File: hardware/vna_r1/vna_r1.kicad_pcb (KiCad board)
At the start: 2 copper layers, 668 parts, among them IC1301 SN74LVC1G07DCK, IC1302 TPD4S012DRYR, IC1303 TPD4S012DRYR, J1202 BARREL_JACK, J1301 RJ45-TRANSFO, J1302 USB_A, J201 BMI-S-209, J401 RF_Shield_Two_Pieces, J402 RF_Shield_Two_Pieces, J501 RF_Shield_Two_Pieces, J601 RF_Shield_Two_Pieces, J701 RF_Shield_Two_Pieces, J801 RF_Shield_Two_Pieces, J901 CONN_01X02, Q1201 Q_PMOS_DGS, Q1301 24 MHz, Q1302 24 MHz, T501 Transformer_SP_1S, T601 Transformer_SP_1S, T701 Transformer_SP_1S, T801 Transformer_SP_1S, U1001 CONN_SMA, U1002 CONN_SMA, U1003 CONN_SMA_2GND, U1004 CONN_SMA_2GND, U1005 CONN_SMA_2GND, U1006 CONN_SMA_2GND, U1007 CONN_SMA_2GND, U1008 CONN_SMA_2GND, U1101 AD9577, U1102 NB3N551, U1201 CONN_SMA, U1202 CONN_SMA, U1301 OSD3358-512M-BSM, U1302 74HC244, U1303 LAN8710A, U1304 TPS2051, U1305 MICROSD, U201 LMX2594, U301 LMX2594, U302 LTC2630, U303 ADRF5040, U304 LTC2054HV, U305 MAAM-011100, U401 NC7WZU04, U402 PE42521, U403 MASW-008322-TR1000, U404 PE42521, U501 LTC5549, U502 ad9864, U601 LTC5549, U602 ad9864, U701 LTC5549, U702 ad9864, U801 LTC5549, U802 ad9864, U901 ADP7158, U902 ADP7158, U903 ADP7158, U904 OKR-T/3-W12-C, U905 TPS2041B, U906 LTC1983, X1301 10118192-0001LF, Y1101 26 MHz 7M-26.000MEEQ-T

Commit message: more layout on vna r1
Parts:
- removed C1323, C1326: 100 nF, Capacitors_SMD:C_0402
- added C227: 10 pF, Capacitors_SMD:C_0603, F.Cu at (582.0, 158.0)
- added R213: 51, Resistors_SMD:R_0402, F.Cu at (581.2, 159.9)
- moved C1201 157.0 mm to (351.7, 73.7)
- moved C1202 157.0 mm to (348.5, 88.5)
- moved C901 157.0 mm to (379.8, 88.0)
- moved C902 157.0 mm to (380.0, 31.0)
- moved C903 157.0 mm to (376.8, 57.0)
- moved C904 157.0 mm to (381.3, 36.0)
- moved C905 157.0 mm to (381.9, 54.0)
- moved C906 157.0 mm to (383.2, 81.0)
- moved C907 157.0 mm to (397.2, 33.0)
- moved C908 157.0 mm to (392.8, 60.0)
- moved C909 157.0 mm to (395.8, 90.0)
- moved C910 157.0 mm to (396.2, 29.0)
- moved C911 157.0 mm to (394.8, 53.0)
- moved C912 157.0 mm to (402.2, 90.0)
- moved C913 157.0 mm to (392.8, 31.0)
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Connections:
- RN1305 pad 1: /control/MMC0_D2 -> /control/MMC0_CLK
- RN1305 pad 2: /control/MMC0_D3 -> /control/MMC0_CMD
- RN1305 pad 3: /control/MMC0_CMD -> /control/MMC0_D3
- RN1305 pad 4: /control/MMC0_CLK -> /control/MMC0_D2
- RN1306 pad 1: /control/MMC0_D0 -> (no net)
- RN1306 pad 2: /control/MMC0_D1 -> /control/MMC0_CD
- RN1306 pad 3: /control/MMC0_CD -> /control/MMC0_D1
- RN1306 pad 4: (no net) -> /control/MMC0_D0
- RN201 pad 1: /LO_SYNTH_LOCK -> /LO_SYNTH_CE
- RN201 pad 2: /LO_SPI_SDI -> /LO_SPI_CLK
- RN201 pad 3: /LO_SPI_CLK -> /LO_SPI_SDI
- RN201 pad 4: /LO_SYNTH_CE -> /LO_SYNTH_LOCK
- RN201 pad 5: /LO_SYNTH_CE -> /LO_SYNTH_LOCK
- RN201 pad 6: /LO_SPI_CLK -> /LO_SPI_SDI
- RN201 pad 7: /LO_SPI_SDI -> /LO_SPI_CLK
- RN201 pad 8: /LO_SYNTH_LOCK -> /LO_SYNTH_CE
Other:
- copper layers 2 -> 4
- rule pad_to_mask_clearance: 0.2 -> 0.05

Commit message: layout on vna r1 control board
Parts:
- removed C201, C202, C217, C301, C302, C317, C332, C333, C335, C339, C344, C346, C401, C405, C406, C503, C603, C703, C803, C918, C920, C922, C924, C925: 100 nF, Capacitors_SMD:C_0402
- removed C203, C206, C207, C208, C209, C210, C221, C303, C306, C307, C308, C309, C310, C320, C904, C907, C910, C923: 1 uF, Capacitors_SMD:C_0402
- removed C204, C211, C214, C218, C219, C304, C311, C312, C318, C319, C902, C913, C919, C921: 10 uF, Capacitors_SMD:C_0603
- removed C205, C220, C222, C223, C224, C227: 10 pF, Capacitors_SMD:C_0603
- removed C212, C315: DNP, Capacitors_SMD:C_0402
- removed C213, C316: 1800 pF, Capacitors_SMD:C_0402
- removed C215, C313: 390 pF, Capacitors_SMD:C_0402
- removed C216, C314: 68 nF, Capacitors_SMD:C_0402
- removed C225, C226, C321, C322: 10 nF, Capacitors_SMD:C_0402
- removed C305, C323, C324, C325, C326, C327, C328, C329, C330, C331, C334, C336, C337, C338, C340, C341, C342, C347, C348, C402, C403, C404, C407, C408, C409, C410, C412, C414, C501, C502, C505, C506, C507, C601, C602, C605, C606, C607, C701, C702, C705, C706, C707, C801, C802, C805, C806, C807: 10 pF, Capacitors_SMD:C_0402
- removed C343, C345: 220 nF, Capacitors_SMD:C_0402
- removed C411, C413: 1 uF, Capacitors_SMD:C_0805
- removed C926: 100 pF, Capacitors_SMD:C_0402
- removed D1001, D1002, D201: RED, LEDs:LED_0603
- removed D301, D302, D303: LED_Small, LEDs:LED_0603
- removed D401: 5.1V, Diodes_SMD:SOD-323
- removed D402: LED, LEDs:LED_0603
- removed FL301: 5515LP15A730, vna_footprints:5515LP15A730
- removed FL302: 1810LP07A200, vna_footprints:1810LP07A200
- removed FL303: 3550LP14A300, vna_footprints:3550LP14A300
- removed J201: BMI-S-209, Shielding_Cabinets:Laird_Technologies_BMI-S-209-F_29.36x18.50mm
- removed J401, J402: RF_Shield_Two_Pieces, Shielding_Cabinets:Laird_Technologies_BMI-S-202-F_16.50x16.50mm
- removed J501, J601, J801: RF_Shield_Two_Pieces, Shielding_Cabinets:Laird_Technologies_BMI-S-209-F_29.36x18.50mm
- removed L201, L202, L301, L302: 22 nH, Resistors_SMD:R_0402
- removed L303, L501, L601, L701, L801: BLM15GG471, Resistors_SMD:R_0402
- removed L401, L402: 506WLSN6R00KT236T, vna_footprints:ATC506WLS
- removed L901: L_Small, Resistors_SMD:R_0805
- removed R201, R205, R304, R324: JMP, Resistors_SMD:R_0402
- removed R202, R301, R403, R404: 100, Resistors_SMD:R_0402
- removed R203, R204, R302, R303, R312, R313, R316, R317, R318, R328, R401, R402, R405, R407, R502, R503, R602, R603, R702, R703, R802, R803: 1k, Resistors_SMD:R_0402
- removed R206, R305: 18, Resistors_SMD:R_0402
- removed R207, R306: 68, Resistors_SMD:R_0402
- removed R208, R314, R315, R327, R905, R906: 10k, Resistors_SMD:R_0402
- removed R209, R210, R211, R212, R213, R308, R309, R310, R311, R406, R408: 51, Resistors_SMD:R_0402
- removed R307: 0, Resistors_SMD:R_0402
- removed R319: 9.1k, Resistors_SMD:R_0402
- removed R320: 4.7k, Resistors_SMD:R_0402
- removed R321, R322, R323: DNP, Resistors_SMD:R_0402
- removed R325: 2k, Resistors_SMD:R_0402
- removed R326: 18k, Resistors_SMD:R_0402
- removed R329: 56.2k, Resistors_SMD:R_0402
- removed R330: 68k, Resistors_SMD:R_0402
- removed RN1304: 49.9, pocketbeagle:RN0804
- removed RN201, RN301: RESISTOR.NETWORK-_4_, pocketbeagle:RN0804
- removed T501, T601, T701, T801: Transformer_SP_1S, vna_footprints:5LEAD_BALUN_4p83mm_3p3mm
- removed U1001, U1002: CONN_SMA, vna_footprints:732511150_sma_thin
- removed U1007, U1008: CONN_SMA_2GND, vna_footprints:SMA_901-10512_6p7MIL_FR408_CPW_LAUNCH
- removed U201, U301: LMX2594, Housings_DFN_QFN:QFN-40-1EP_6x6mm_Pitch0.5mm
- removed U302: LTC2630, TO_SOT_Packages_SMD:SC-70-6
- removed U303: ADRF5040, Housings_DFN_QFN:QFN-24-1EP_4x4mm_Pitch0.5mm
- removed U304: LTC2054HV, TO_SOT_Packages_SMD:SOT-23-5
- removed U305: MAAM-011100, vna_footprints:TDFN6
- removed U401: NC7WZU04, TO_SOT_Packages_SMD:SC-70-6
- removed U402, U404: PE42521, Housings_DFN_QFN:QFN-16-1EP_3x3mm_Pitch0.5mm
- removed U403: MASW-008322-TR1000, Housings_DFN_QFN:QFN-24-1EP_4x4mm_Pitch0.5mm
- removed U501, U601, U701, U801: LTC5549, vna_footprints:QFN_12_3mm2mm
- removed U901: ADP7158, Housings_DFN_QFN:DFN-10-1EP_3x3mm_Pitch0.5mm
- removed U905: TPS2041B, TO_SOT_Packages_SMD:SOT-23-5
- removed U906: LTC1983, TO_SOT_Packages_SMD:SOT-23-6
- added H901: MOUNTING_HOLE, Mounting_Holes:MountingHole_2-7mm, F.Cu at (297.6, -102.4)
- added H902: MOUNTING_HOLE, Mounting_Holes:MountingHole_2-7mm, F.Cu at (423.5, -109.5)
- added H903: MOUNTING_HOLE, Mounting_Holes:MountingHole_2-7mm, F.Cu at (422.4, -185.4)
- added H904: MOUNTING_HOLE, Mounting_Holes:MountingHole_2-7mm, F.Cu at (309.0, -183.6)
- added J1201: DB15_FEMALE_MountingHoles, Connect:DB15FD, F.Cu at (409.4, -89.4)
- added R1004: 51, Resistors_SMD:R_0402, F.Cu at (314.2, -146.7)
- added R1005: 51, Resistors_SMD:R_0402, F.Cu at (314.2, -143.8)
- C1314, RN1305, RN1306: moved to B.Cu
- J1301: value RJ45-TRANSFO -> 0480254000; footprint Connect:RJHSE538X -> Connect:RJ45_TRANSFO
- J701: value RF_Shield_Two_Pieces -> Conn_01x07; footprint Shielding_Cabinets:Laird_Technologies_BMI-S-209-F_29.36x18.50mm -> Connect:Wafer_Horizontal20x5.8x7RM2.5-7
- R1001, R1002: value 1k -> 51
- TP1301, TP1302, TP1303, TP1304, TP1305, TP1306, TP1307, TP1308, TP1309, TP1310: footprint pocketbeagle:TP07R -> vna_footprints:TP07R
- moved U1006 459.4 mm to (409.3, -195.3), turned to 90 degrees
- moved R1002 457.7 mm to (314.2, -149.2), turned to 90 degrees
- moved R1001 448.1 mm to (314.2, -151.7), turned to 270 degrees
- moved C804 439.5 mm to (394.5, -186.3), turned to 90 degrees
- moved D1003 438.1 mm to (319.1, -115.1), turned to 90 degrees
- moved R1003 436.4 mm to (318.8, -112.1), turned to 270 degrees
- moved C808 433.9 mm to (400.8, -184.3)
- moved R805 431.6 mm to (400.0, -181.4), turned to 90 degrees
- moved C823 430.6 mm to (407.6, -174.4)
- moved R801 429.8 mm to (394.5, -183.6), turned to 270 degrees
- moved R806 427.1 mm to (404.0, -176.7), turned to 180 degrees
- moved R812 424.8 mm to (389.8, -167.5), turned to 180 degrees
- moved C824 422.4 mm to (412.8, -175.5), turned to 90 degrees
- moved C815 422.3 mm to (405.0, -168.9), turned to 180 degrees
- moved C813 420.4 mm to (403.3, -171.3), turned to 270 degrees
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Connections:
- C504 pad 2: Net-(C504-Pad2) -> /front_panel/DEMOD_1
- C604 pad 2: Net-(C604-Pad2) -> /front_panel/DEMOD_2
- C704 pad 2: Net-(C704-Pad2) -> /front_panel/DEMOD_3
- C804 pad 2: Net-(C804-Pad2) -> /front_panel/DEMOD_4
- J701 pad 1: GND -> (no net)
- L1304 pad 2: (no net) -> Net-(J1301-Pad13)
- R1001 pad 1: Net-(D1001-Pad1) -> Net-(C1311-Pad1)
- R1001 pad 2: GND -> /control/RX_N
- R1002 pad 1: Net-(D1002-Pad1) -> Net-(C1311-Pad1)
- R1002 pad 2: GND -> /control/RX_P
- R1355 pad 2: (no net) -> Net-(J1301-PadGK)
- R1356 pad 2: (no net) -> Net-(J1301-PadYK)
- U1101 pad 17: /SYNTH_REF_AN -> (no net)
- U1101 pad 18: /SYNTH_REF_AP -> (no net)
- U1101 pad 22: /SYNTH_REF_BN -> (no net)
- U1101 pad 23: /SYNTH_REF_BP -> (no net)
- U1301 pad A10: /RF_AMP_EN -> (no net)
- U1301 pad A13: (no net) -> /EXT_SPI_MOSI
- U1301 pad A14: (no net) -> /EXT_SPI_CS0
- U1301 pad A2: /RF_SYNTH_CS -> (no net)
- U1301 pad A3: /LO_SPI_CLK -> (no net)
- U1301 pad B1: /RF_DAC_CS -> (no net)
- U1301 pad B13: (no net) -> /EXT_SPI_MISO
- U1301 pad B14: (no net) -> /EXT_SPI_CLK
- U1301 pad B2: /LO_SYNTH_CS -> (no net)
- U1301 pad B3: /LO_SPI_SDI -> (no net)
- U1301 pad B4: /-5V_EN -> (no net)
- U1301 pad C12: /3V3_RF_EN -> (no net)
- U1301 pad C3: /RF_SPI_CLK -> (no net)
- U1301 pad C4: /RF_SPI_SDI -> (no net)
- U1301 pad C8: (no net) -> /EXT_AIN0
- U1301 pad C9: (no net) -> /EXT_AIN1
- U1301 pad E1: (no net) -> Net-(TP1308-Pad1)
- U1301 pad F13: (no net) -> Net-(TP1303-Pad1)
- U1301 pad F2: (no net) -> Net-(TP1307-Pad1)
- U1301 pad F4: (no net) -> Net-(TP1301-Pad1)
- U1301 pad G13: (no net) -> Net-(TP1304-Pad1)
- U1301 pad G4: (no net) -> Net-(TP1302-Pad1)
- U1301 pad N13: (no net) -> Net-(TP1309-Pad1)
- U1301 pad P1: (no net) -> /EXT_IO_2
- U1301 pad P2: (no net) -> /EXT_IO_1
- U1301 pad P3: (no net) -> /EXT_IO_0
- U1301 pad P4: /LO_SYNTH_LOCK -> (no net)
- U1301 pad R1: /RF_FILT_SW_1 -> (no net)
- U1301 pad R12: /MIX_EN -> (no net)
- U1301 pad R13: /PANEL_PORT1_LED -> (no net)
- U1301 pad R4: /LO_SYNTH_CE -> (no net)
- U1301 pad R7: (no net) -> /EXT_IO_3
- U1301 pad T1: /RF_SYNTH_LOCK -> (no net)
- U1301 pad T12: /MIX_X2 -> (no net)
- U1301 pad T15: /PANEL_PORT2_LED -> (no net)
- U1301 pad T2: /RF_SYNTH_CE -> (no net)
- U1301 pad T3: /RF_FILT_SW_2 -> (no net)
- U1301 pad T7: (no net) -> /EXT_SPI_CS1
- U1303 pad 2: (no net) -> /control/ETH_LEDY
- U1303 pad 3: (no net) -> /control/ETH_LEDG
- U902 pad 3: /3V3_DEMOD_SENSE -> (no net)
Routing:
- net Net-(L1307-Pad1): track 0.00 -> 36.9 mm
- net Net-(C1311-Pad1): track 0.00 -> 28.0 mm, vias 0 -> 5
- net /control/ETH_LEDY: track 0.00 -> 27.0 mm, vias 0 -> 1
- net Net-(J1301-Pad13): track 0.00 -> 26.4 mm
- net GND: track 0.00 -> 25.2 mm, vias 0 -> 35
- net /control/ETH_LEDG: track 0.00 -> 22.3 mm, vias 0 -> 2
- net Net-(C1315-Pad1): track 0.00 -> 21.2 mm
- net /control/RX_N: track 0.00 -> 20.2 mm, vias 0 -> 2
- net Net-(J1302-Pad5): track 0.00 -> 19.8 mm
- net /control/RX_P: track 0.00 -> 18.9 mm, vias 0 -> 2
- net VDD_3V3B: track 0.00 -> 18.6 mm, vias 0 -> 4
- net Net-(L1303-Pad1): track 0.00 -> 15.9 mm
- net /control/TX_P: track 0.00 -> 14.9 mm
- net /control/TX_N: track 0.00 -> 14.3 mm
- net VDD_5V: track 0.00 -> 12.3 mm
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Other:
- board outline added: 193.6 x 98.5 mm
- net class Default: clearance 0.2 -> 0.1524; trace_width 0.25 -> 0.1524
- rule trace_clearance: 0.2 -> 0.1524
- rule trace_min: 0.2 -> 0.1524
- board text added: "todo: - fix SATA connector footprint - find board to board data connector"

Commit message: added adrf5020 breakout
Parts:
- removed C1201: 470 uF, Capacitors_SMD:c_elec_6.3x5.8
- removed D1003: RED, LEDs:LED_0603
- removed R1003: 1k, Resistors_SMD:R_0402
- U1003, U1004, U1005, U1006: footprint vna_footprints:SMA_901-10512_6p7MIL_FR408_CPW_LAUNCH -> vna_footprints:732511150_sma_thin
- moved U1202 59.2 mm to (377.6, -196.8)
- moved C525 49.5 mm to (467.9, -212.6)
- moved C527 49.5 mm to (467.9, -207.1)
- moved C536 49.5 mm to (509.2, -224.8)
- moved C619 49.5 mm to (497.6, -80.9)
- moved C623 49.5 mm to (499.7, -59.1)
- moved C625 49.5 mm to (505.0, -86.5)
- moved C629 49.5 mm to (492.2, -51.6)
- moved C632 49.5 mm to (505.0, -81.1)
- moved C637 49.5 mm to (499.7, -64.5)
- moved C715 49.5 mm to (489.2, -138.0)
- moved C716 49.5 mm to (493.4, -143.4)
- moved C719 49.5 mm to (473.3, -144.1)
- moved C727 49.5 mm to (473.3, -149.6)
- moved C728 49.5 mm to (491.1, -161.4)
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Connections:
- U1301 pad F3: (no net) -> /3V3_DEMOD_EXT_EN
- U1301 pad R13: (no net) -> /3V3_DEMOD_EXT_EN
- U1301 pad T13: /PANEL_POWER_LED -> (no net)
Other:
- board size 193.6 x 98.5 mm -> 193.6 x 99.7 mm

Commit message: more work on vna r1..
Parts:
- added L601: L_Small, Resistors_SMD:R_0402, F.Cu at (347.0, -112.2)
- C1103, C1106, C1107, C1109, C1120, C1122, C1123, C1303, C1304, C1325, Q1301, R1325, R1354, U1304: moved to B.Cu
- moved U1202 88.5 mm to (367.8, -108.8), turned to 0 degrees
- moved C835 45.3 mm to (401.6, -196.4)
- moved R812 45.3 mm to (400.1, -201.4)
- moved R813 45.3 mm to (402.3, -201.9)
- moved C804 37.6 mm to (405.2, -200.7)
- moved R801 37.6 mm to (405.2, -198.0)
- moved R1326 34.3 mm to (336.5, -154.8), turned to 270 degrees
- moved R1118 31.5 mm to (338.1, -174.2), turned to 0 degrees
- moved R1301 28.6 mm to (335.0, -154.7), turned to 90 degrees
- moved R1328 26.8 mm to (359.5, -144.7), turned to 270 degrees
- moved D1302 25.8 mm to (312.2, -180.2)
- moved D1303 25.8 mm to (312.2, -181.8)
- moved D1304 25.8 mm to (312.2, -183.5)
- moved D1305 25.8 mm to (312.2, -185.0)
- moved RN1301 25.8 mm to (308.9, -182.5)
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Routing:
- net /control/USB_DEV_DM: track 7.30 -> 26.3 mm
- net VDD_5V: track 12.3 -> 4.17 mm
- net /control/USB1_DRVVBUS: track 4.09 -> 0.00 mm
- net GND: track 25.2 -> 22.5 mm, vias 35 -> 32
- net /control/USB_HOST_DP: track 7.83 -> 5.83 mm
- net /control/USB_DEV_DP: track 7.40 -> 9.37 mm
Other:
- board size 193.6 x 99.7 mm -> 193.6 x 114.8 mm

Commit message: work on vna r1 synth board
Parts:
- removed J701: Conn_01x07, Connect:Wafer_Horizontal20x5.8x7RM2.5-7
- added J1001: Conn_02x10_Odd_Even, Connect:IDC_Header_Straight_20pins, F.Cu at (325.0, -71.8)
- added J1002: Conn_02x10_Odd_Even, Connect:IDC_Header_Straight_20pins, F.Cu at (360.7, -71.9)
- added J1003: Conn_02x04_Odd_Even, Pin_Headers:Pin_Header_Straight_2x04, F.Cu at (329.0, -83.3)
- added R702, R714, R715, R716, R717: DNP, Resistors_SMD:R_0402, F.Cu at (305.3, -197.5)
- added R703: 10k, Resistors_SMD:R_0402, F.Cu at (305.3, -197.5)
- added U1001: CONN_SMA_2GND, vna_footprints:734120110_ufl_umc, F.Cu at (302.8, -204.5)
- added U1002: CONN_SMA_2GND, vna_footprints:734120110_ufl_umc, F.Cu at (314.3, -204.3)
- added U1007: CONN_SMA_2GND, vna_footprints:734120110_ufl_umc, F.Cu at (298.0, -204.4)
- added U1008: CONN_SMA_2GND, vna_footprints:734120110_ufl_umc, F.Cu at (309.4, -204.3)
- J1201: footprint Connect:DB15FD -> vna_footprints:DB15MC
- moved J1201 103.4 mm to (306.1, -86.8), turned to 90 degrees
- moved TP1301 57.0 mm to (328.3, -48.6)
- moved TP1302 57.0 mm to (327.7, -54.8)
- moved TP1303 57.0 mm to (317.7, -53.8)
- moved TP1304 57.0 mm to (328.3, -45.7)
- moved TP1305 57.0 mm to (324.7, -60.8)
- moved TP1306 57.0 mm to (315.4, -31.4)
- moved TP1307 57.0 mm to (322.9, -31.4)
- moved TP1308 57.0 mm to (323.2, -36.8)
- moved TP1309 57.0 mm to (316.2, -40.0)
- moved TP1310 57.0 mm to (318.2, -47.8)
- moved U1202 49.0 mm to (398.0, -70.2)
- moved H901 37.0 mm to (313.1, -72.2)
- moved R1319 36.0 mm to (358.2, -139.2)
- moved R1307 36.0 mm to (358.4, -145.0), turned to 180 degrees
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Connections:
- net /PORT_SEL renamed /RF_PORT_SEL
- U1101 pad 17: (no net) -> /SYNTH_REF_AN
- U1101 pad 18: (no net) -> /SYNTH_REF_AP
- U1101 pad 22: (no net) -> /SYNTH_REF_BN
- U1101 pad 23: (no net) -> /SYNTH_REF_BP
- U1301 pad A10: (no net) -> /RF_AMP_EN
- U1301 pad A2: (no net) -> /RF_SYNTH_CS
- U1301 pad A3: (no net) -> /LO_SPI_CLK
- U1301 pad B1: (no net) -> /RF_DAC_CS
- U1301 pad B2: (no net) -> /LO_SYNTH_CS
- U1301 pad B3: (no net) -> /LO_SPI_SDI
- U1301 pad B4: (no net) -> /RF_-5V_EN
- U1301 pad C12: (no net) -> /RF_3V3_EN
- U1301 pad C3: (no net) -> /RF_SPI_CLK
- U1301 pad C4: (no net) -> /RF_SPI_SDI
- U1301 pad P4: (no net) -> /LO_SYNTH_LOCK
- U1301 pad R1: (no net) -> /RF_FILT_SW_1
- U1301 pad R12: (no net) -> /MIX_EN
- U1301 pad R4: (no net) -> /LO_SYNTH_CE
- U1301 pad T1: (no net) -> /RF_SYNTH_LOCK
- U1301 pad T12: (no net) -> /MIX_X2
- U1301 pad T2: (no net) -> /RF_SYNTH_CE
- U1301 pad T3: (no net) -> /RF_FILT_SW_2
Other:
- board size 193.6 x 114.8 mm -> 193.6 x 146.5 mm
- board text removed: "todo: - fix SATA connector footprint - find board to board data connector"

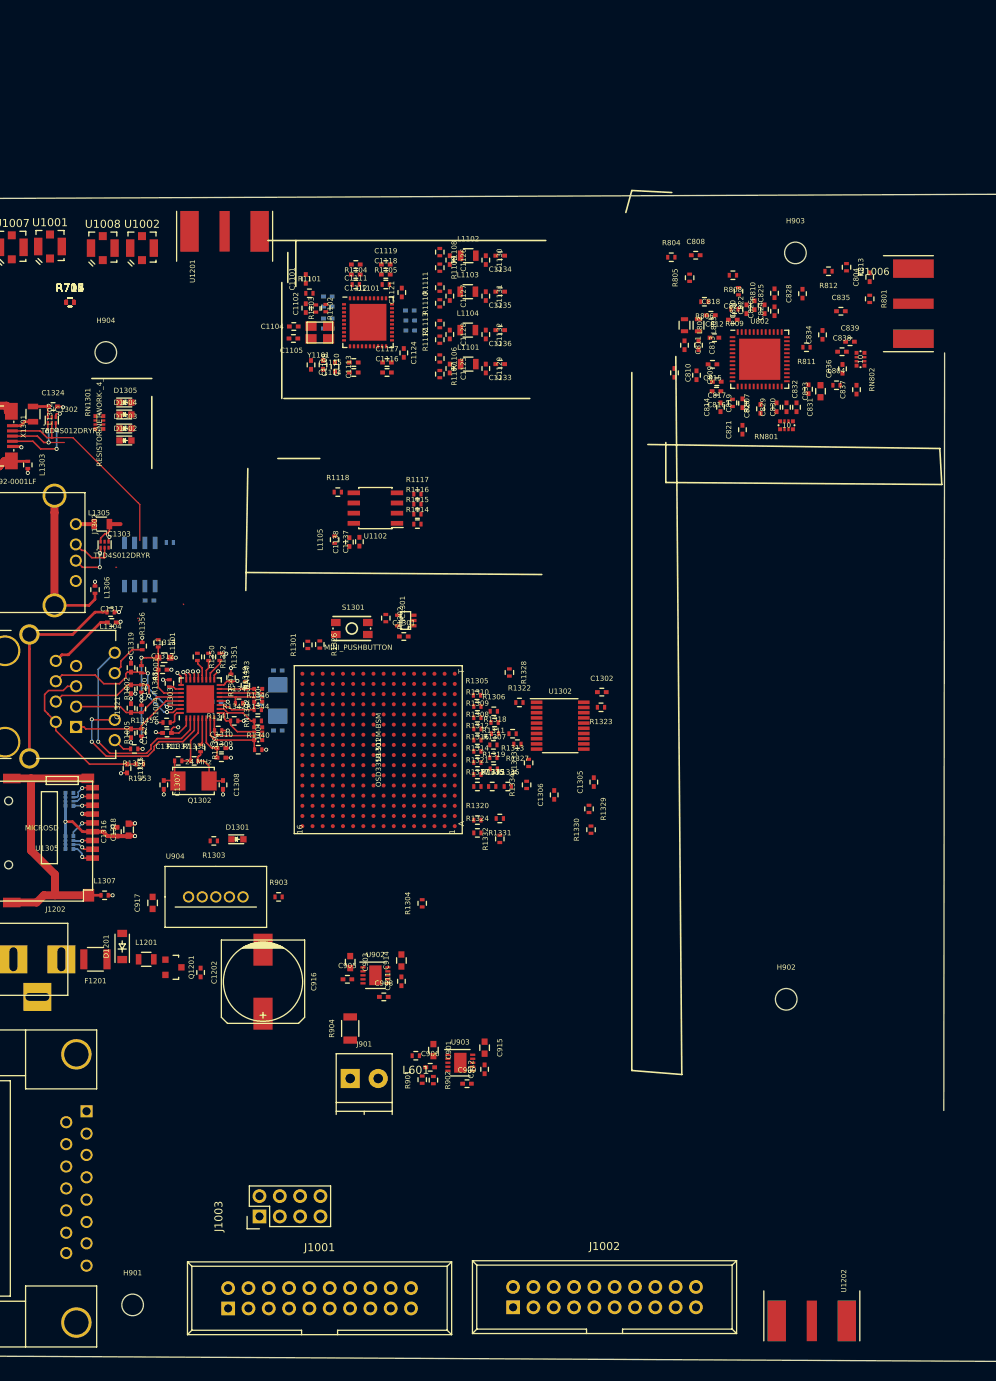
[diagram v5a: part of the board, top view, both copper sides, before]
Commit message: ethernet and usb layout on vna control board..
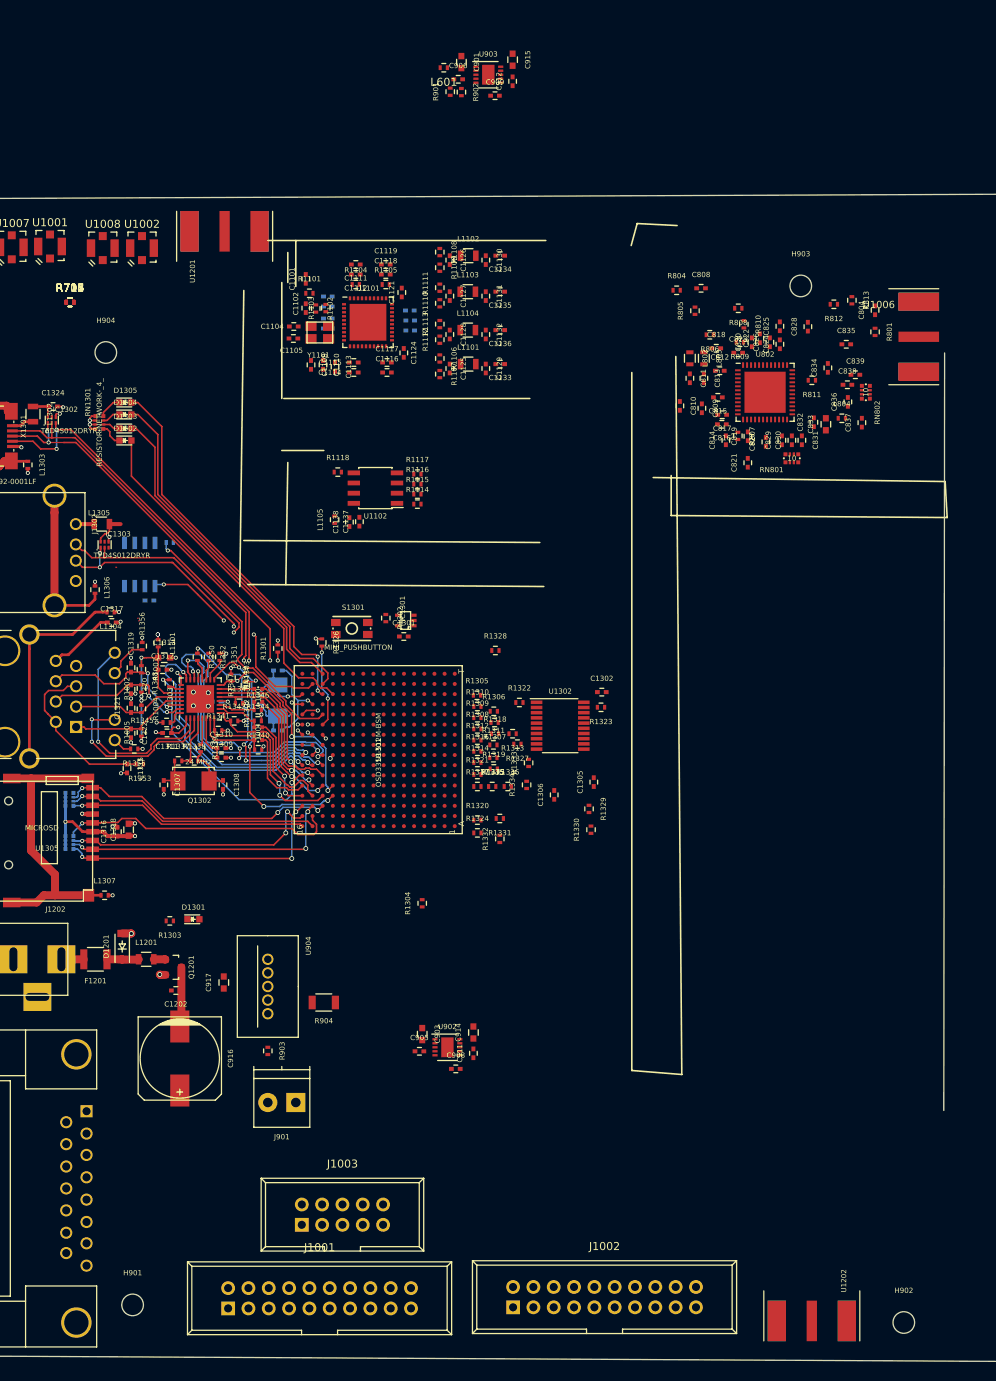
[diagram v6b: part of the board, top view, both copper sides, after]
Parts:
- J1003: value Conn_02x04_Odd_Even -> Conn_02x05_Odd_Even; footprint Pin_Headers:Pin_Header_Straight_2x04 -> Connect:IDC_Header_Straight_10pins
- moved C901 123.5 mm to (354.2, -227.6)
- moved R902 123.5 mm to (354.2, -223.8)
- moved C906 123.5 mm to (353.8, -225.4)
- moved C909 123.5 mm to (358.4, -223.3)
- moved C912 123.5 mm to (360.6, -225.2)
- moved C915 123.5 mm to (360.6, -227.8)
- moved L601 123.5 mm to (352.0, -226.8)
- moved R901 123.5 mm to (352.8, -223.8)
- moved U903 123.5 mm to (357.6, -226.0)
- moved H902 43.0 mm to (409.5, -70.0)
- moved R903 19.3 mm to (330.0, -104.0), turned to 270 degrees
- moved C916 14.2 mm to (319.0, -103.0)
- moved C917 13.3 mm to (324.5, -112.5)
- moved U904 12.9 mm to (330.0, -112.0), turned to 270 degrees
- moved C903 12.7 mm to (349.3, -106.0)
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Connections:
- J1001 pad 11: (no net) -> /LO_AMP_EN
- J1003 pad 1: GND -> +5V
- J1003 pad 2: /MIX_X2 -> +5V
- J1003 pad 3: GND -> +5V
- J1003 pad 4: /MIX_EN -> GND
- J1003 pad 5: VPP -> GND
- J1003 pad 7: VPP -> GND
- J1003 pad 8: GND -> /LO_AMP_EN
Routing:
- net /control/USB_DEV_ID: track 9.19 -> 63.4 mm, vias 2 -> 4
- net /control/USB_DEV_DP: track 9.37 -> 61.3 mm, vias 2 -> 4
- net /control/USR3_LED: track 0.00 -> 48.0 mm, vias 0 -> 2
- net /control/USR2_LED: track 0.00 -> 45.6 mm
- net /control/USR0_LED: track 0.00 -> 43.6 mm
- net /control/USR1_LED: track 0.00 -> 41.8 mm
- net /control/USB_HOST_DP: track 5.83 -> 43.3 mm, vias 2 -> 4
- net /control/USB_HOST_DM: track 5.54 -> 43.0 mm, vias 0 -> 2
- net /control/MII_TXD0: track 1.12 -> 35.2 mm, vias 1 -> 4
- net /control/USB1_DRVVBUS: track 0.00 -> 33.2 mm, vias 0 -> 1
- net /control/USB_DEV_DM: track 26.3 -> 59.1 mm, vias 0 -> 2
- net /control/MMC0_D3: track 2.65 -> 35.0 mm, vias 1 -> 3
- net /control/MMC0_D2: track 3.11 -> 35.2 mm, vias 1 -> 3
- net /control/MII_TXD1: track 1.20 -> 32.8 mm, vias 1 -> 2
- net /control/MMC0_CLK: track 3.38 -> 34.7 mm
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- added copper zone on In1.Cu, net GND
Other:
- net class Default: via_dia 0.6 -> 0.505; via_drill 0.4 -> 0.3
